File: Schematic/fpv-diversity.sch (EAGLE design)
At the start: 63 parts, among them U1 LM1881M/NOPB, U2 LM1881M/NOPB, U3 LM1881M/NOPB, U4 MAX4545CAP+, U5 LT6206CMS8PBF, U6 LM1117IMP-5.0-NOPB

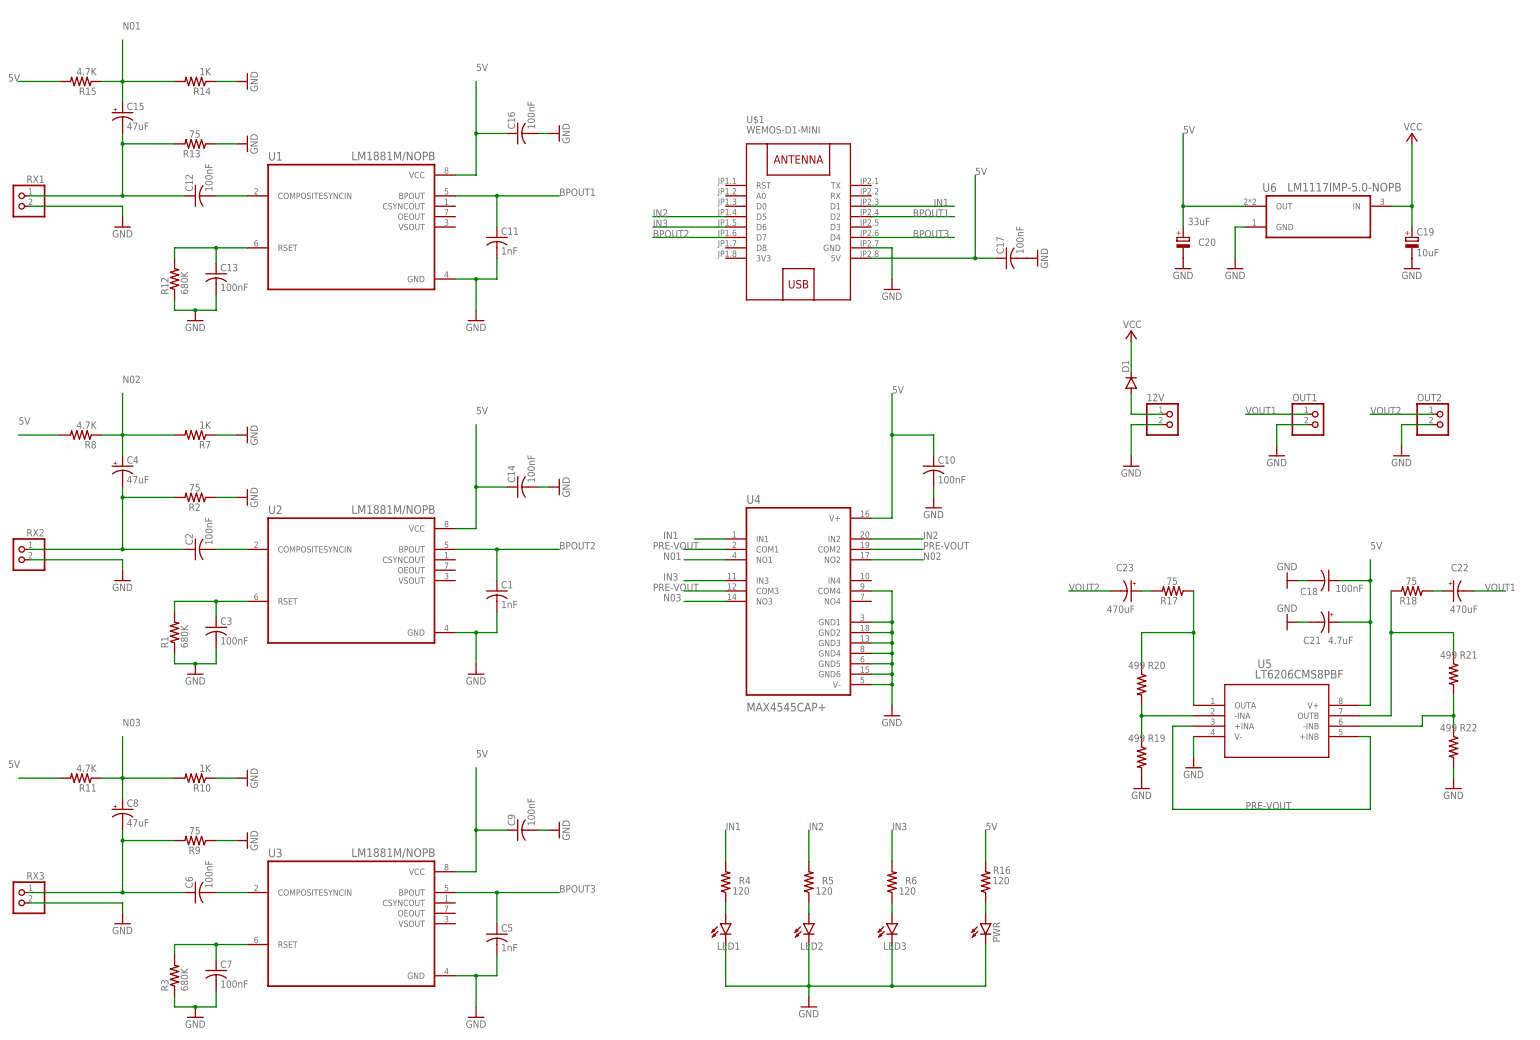
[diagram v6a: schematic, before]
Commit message: board gerber updates
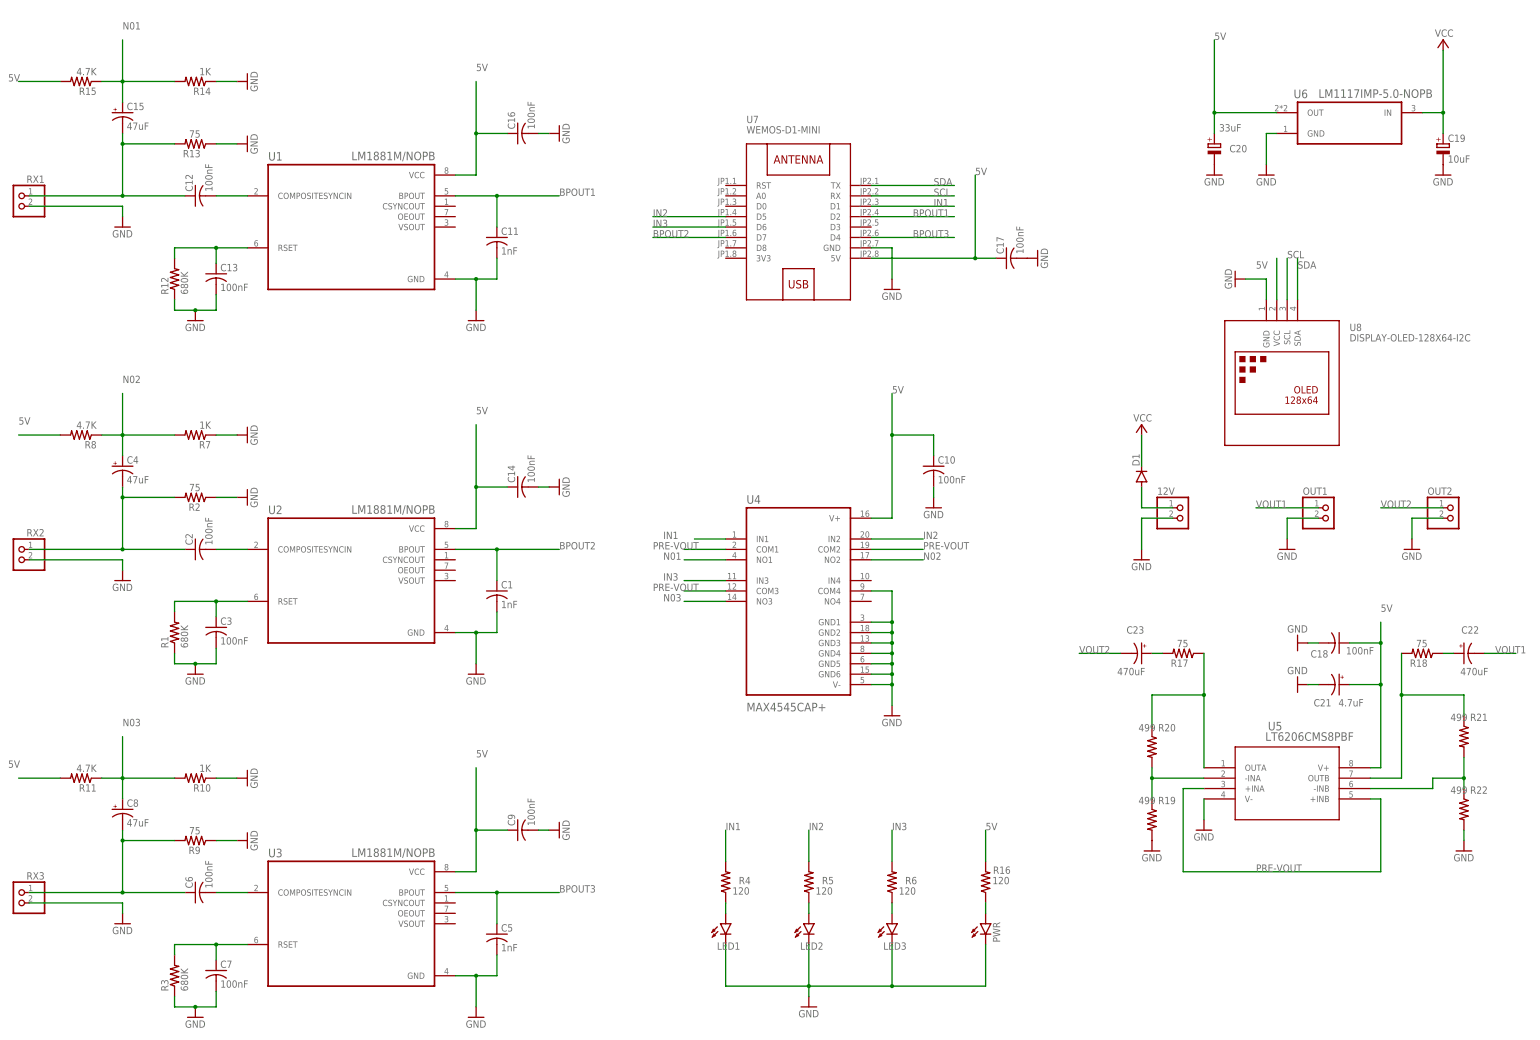
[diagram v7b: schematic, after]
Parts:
- added U8: DISPLAY-OLED-128X64-I2C, DISPLAY-OLED-128X64-I2C-3D:DISPLAY-OLED-128X64-I2C
- renumbered U$1 to U7
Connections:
- new net SCL: U7.RX, U8.SCL
- new net SDA: U7.TX, U8.SDA
- net 5V: now also U8.VCC
- net GND: now also U8.GND
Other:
- moved on the sheet: 12V, C18, C19, C20, C21, C22, C23, D1, OUT1, OUT2, R17, R18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
